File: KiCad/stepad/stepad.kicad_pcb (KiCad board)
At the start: 2 copper layers, 111.2 x 35 mm, 69 parts, among them J1 TYPE-C-31-M12_13_EDITED, J2 Conn_01x03, SW1 MX_Lekker, SW2 MX_Lekker, SW3 MX_Lekker, SW4 MX_Lekker, SW5 SW_Push, SW6 SW_Push, U1 AH49-E, U2 AH49-E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

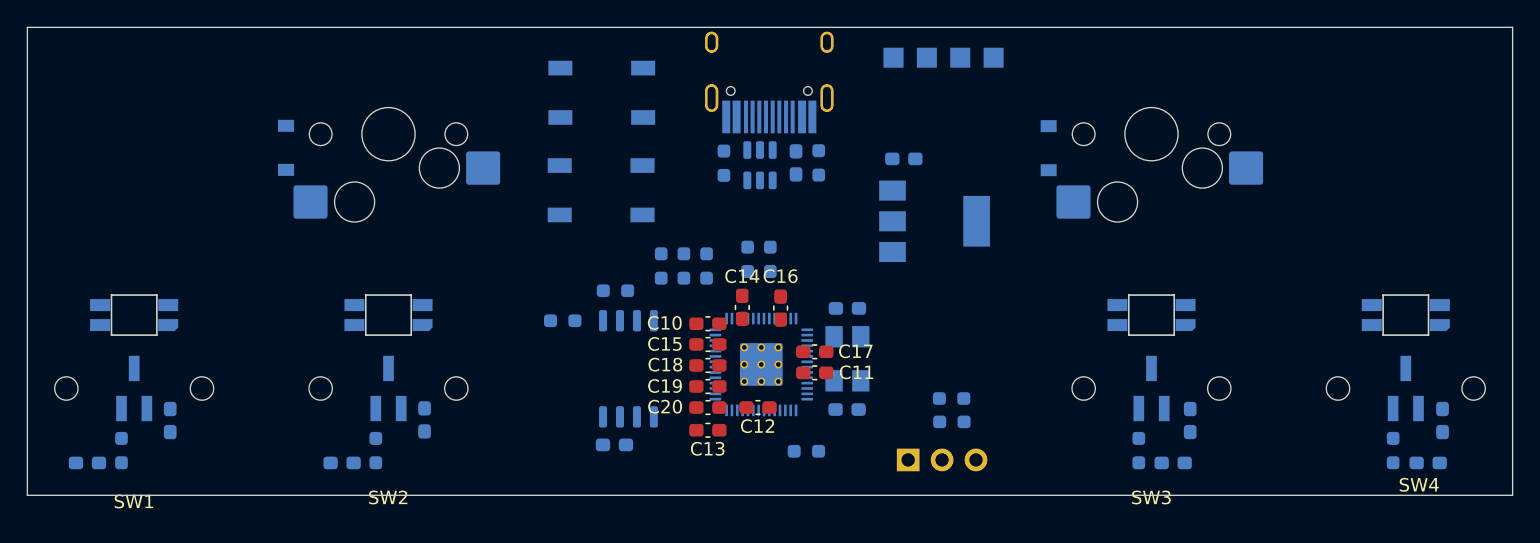
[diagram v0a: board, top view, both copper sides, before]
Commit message: Finished initial layout
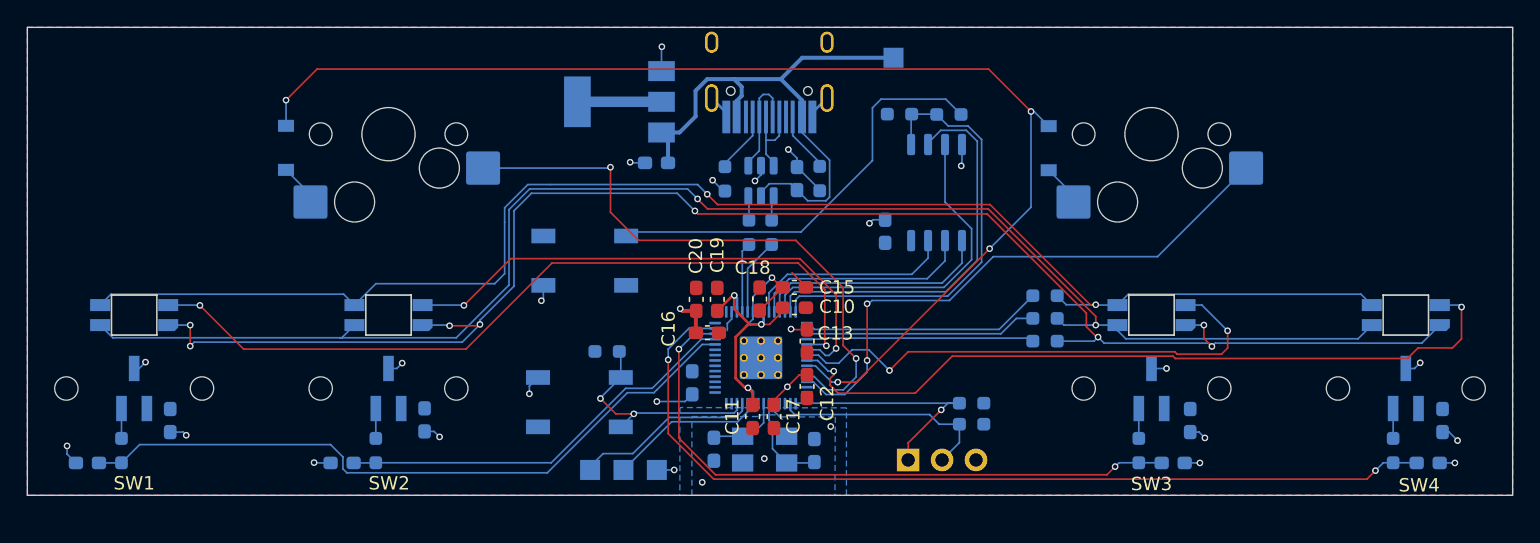
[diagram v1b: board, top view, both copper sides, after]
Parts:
- C14: moved to B.Cu
- moved TP2 39.9 mm to (184.6, 78.1)
- moved TP3 39.9 mm to (187.1, 78.1)
- moved TP4 39.9 mm to (189.6, 78.1)
- moved R11 32.8 mm to (211.4, 51.5), turned to 180 degrees
- moved R5 28.8 mm to (218.6, 65.0), turned to 0 degrees
- moved R6 27.3 mm to (218.6, 66.8), turned to 0 degrees
- moved U6 26.6 mm to (210.5, 57.3)
- moved R7 26.0 mm to (218.6, 68.5), turned to 180 degrees
- moved C21 25.8 mm to (206.7, 60.2), turned to -90 degrees
- moved U5 25.2 mm to (186.8, 50.5), turned to 180 degrees
- moved R10 25.1 mm to (207.7, 51.5), turned to 180 degrees
- moved SW6 23.2 mm to (183.8, 73.0)
- moved C5 18.5 mm to (189.5, 55.1), turned to 0 degrees
- moved R16 16.7 mm to (185.8, 69.2)
- moved C22 10.9 mm to (201.3, 76.7), turned to -90 degrees
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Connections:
- SW6 pad 2: GND -> (no net)
- SW6 pad 3: (no net) -> /RESET
- SW6 pad 4: (no net) -> GND
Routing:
- net Net-(D1-Pad1): track 0.00 -> 121.8 mm, vias 0 -> 8
- net Net-(D1-Pad2): track 0.00 -> 113.8 mm, vias 0 -> 2
- net Net-(D1-Pad3): track 0.00 -> 110.1 mm, vias 0 -> 2
- net K_ROW: track 0.00 -> 91.7 mm, vias 0 -> 4
- net SW4: track 0.00 -> 68.5 mm, vias 0 -> 2
- net COL1: track 0.00 -> 59.8 mm, vias 0 -> 2
- net COL4: track 0.00 -> 57.0 mm, vias 0 -> 2
- net SW1: track 0.00 -> 52.1 mm
- net SW3: track 0.00 -> 47.5 mm, vias 0 -> 2
- net K_COL0: track 0.00 -> 44.3 mm, vias 0 -> 2
- net K_COL1: track 0.00 -> 43.3 mm, vias 0 -> 2
- net +5V: track 0.00 -> 43.2 mm
- net GND: track 0.00 -> 41.0 mm, vias 0 -> 26
- net COL2: track 0.00 -> 40.2 mm, vias 0 -> 2
- net COL3: track 0.00 -> 38.9 mm, vias 0 -> 2
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- added copper zone on B.Cu, net +3.3VA
- added copper zone on B.Cu, net GND
- added copper zone on F.Cu, net GND

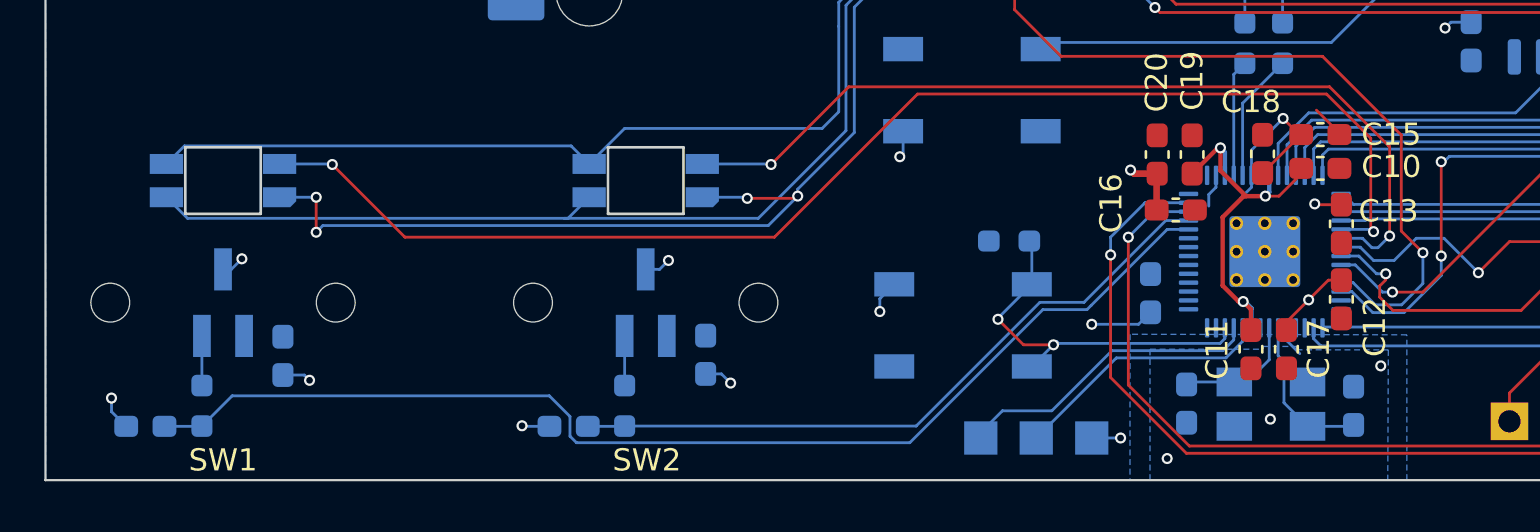
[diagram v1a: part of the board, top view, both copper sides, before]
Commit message: Adding part numbers and updating some footprints
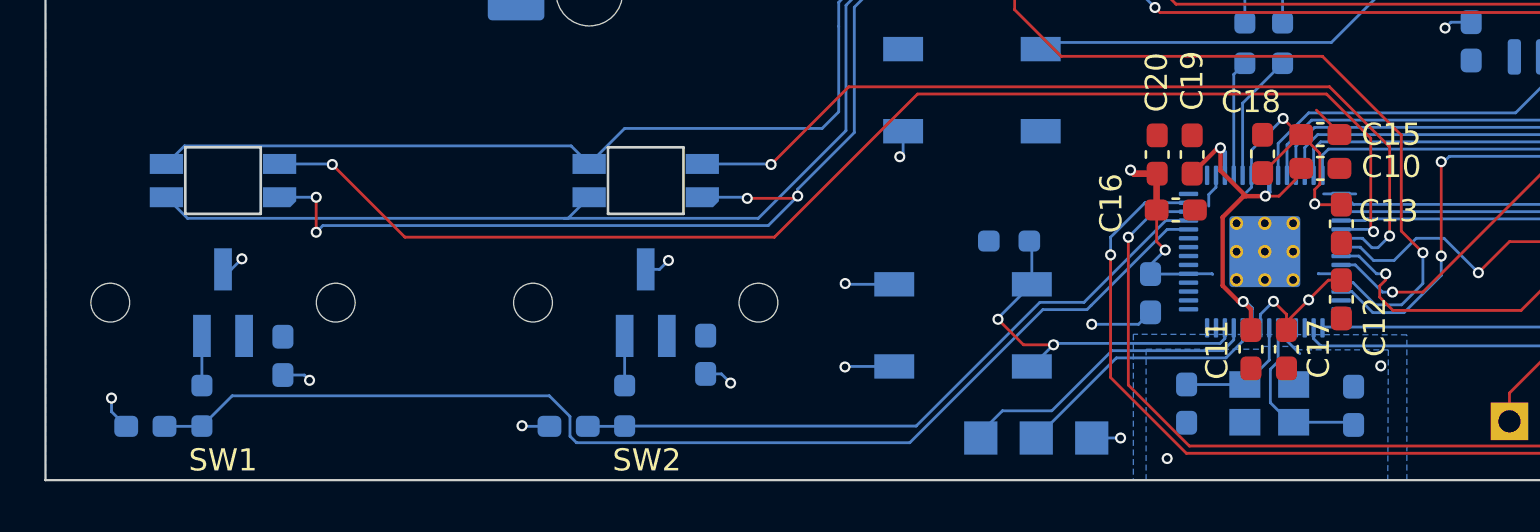
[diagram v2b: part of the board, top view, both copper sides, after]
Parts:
- Y1: footprint Crystal:Crystal_SMD_5032-4Pin_5.0x3.2mm -> Crystal:Crystal_SMD_3225-4Pin_3.2x2.5mm
- moved Y1 0.08 mm to (197.6, 76.5)
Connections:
- SW6 pad 2: (no net) -> GND
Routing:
- net +3.3VA: track 23.6 -> 38.7 mm, vias 4 -> 6
- net GND: track 41.0 -> 44.0 mm
- net /XOUT: track 5.62 -> 6.39 mm
- net /XIN: track 7.09 -> 7.68 mm

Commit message: Updating gerbers and adding firmware folder
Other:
- board text added: "RX"
- board text added: "TX"
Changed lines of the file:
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@@
   )
   (gr_rect (start 253.65 80) (end 142.4 44.95) (layer "Edge.Cuts") (width 0.1) (fill none))
+  (gr_text "RX" (at 210.89 75.23) (layer "F.SilkS")
+    (effects (font (size 1 1) (thickness 0.15)))
+  )
+  (gr_text "TX" (at 208.27 75.27) (layer "F.SilkS")
+    (effects (font (size 1 1) (thickness 0.15)))
+  )
   (segment (start 198.175 63.7) (end 198.9 64.425) (width 0.127) (layer "F.Cu") (net 1))
   (segment (start 192.475 67.825) (end 192.475 66.2125) (width 0.3) (layer "F.Cu") (net 1))
@@
   (segment (start 243.375 78.15) (end 243.9625 77.5625) (width 0.127) (layer "B.Cu") (net 6))
   (segment (start 195.2375 65.025) (end 194.075 66.1875) (width 0.2) (layer "F.Cu") (net 7))
-  (segment (start 198.9875 66.2) (end 197.9875 67.2) (width 0.127) (layer "F.Cu") (net 7))
   (segment (start 196.166793 71.95) (end 195.450479 71.233686) (width 0.2) (layer "F.Cu") (net 7))
   (segment (start 196.4 67.2) (end 196.5 67.2) (width 0.2) (layer "F.Cu") (net 7))
+  (segment (start 197.35 67.4) (end 196.7 67.4) (width 0.2) (layer "F.Cu") (net 7))
   (segment (start 196.5 67.2) (end 195.35 66.05) (width 0.2) (layer "F.Cu") (net 7))
   (segment (start 195.35 66.05) (end 195.35 65.025) (width 0.2) (layer "F.Cu") (net 7))
-  (segment (start 197.375 67.2) (end 196.5 67.2) (width 0.2) (layer "F.Cu") (net 7))
+  (segment (start 198.9875 66.2) (end 198.9875 65.95) (width 0.127) (layer "F.Cu") (net 7))
   (segment (start 195.450479 68.149521) (end 196.4 67.2) (width 0.2) (layer "F.Cu") (net 7))
   (segment (start 195.450479 71.233686) (end 195.450479 68.149521) (width 0.2) (layer "F.Cu") (net 7))
   (segment (start 196.375 71.95) (end 196.725 72.3) (width 0.2) (layer "F.Cu") (net 7))
-  (segment (start 198.9875 65.95) (end 198.9875 66.2) (width 0.127) (layer "F.Cu") (net 7))
+  (segment (start 196.7 67.4) (end 196.5 67.2) (width 0.2) (layer "F.Cu") (net 7))
   (segment (start 195.35 65.025) (end 195.2375 65.025) (width 0.2) (layer "F.Cu") (net 7))
   (segment (start 196.725 72.3) (end 196.725 73.2375) (width 0.2) (layer "F.Cu") (net 7))
   (segment (start 196.375 71.95) (end 196.166793 71.95) (width 0.2) (layer "F.Cu") (net 7))
-  (segment (start 197.375 67.2) (end 197.9875 67.2) (width 0.127) (layer "F.Cu") (net 7))
+  (segment (start 197.7875 67.4) (end 198.9875 66.2) (width 0.127) (layer "F.Cu") (net 7))
+  (segment (start 197.35 67.4) (end 197.7875 67.4) (width 0.127) (layer "F.Cu") (net 7))
   (via (at 195.35 65.025) (size 0.5) (drill 0.3) (layers "F.Cu" "B.Cu") (net 7))
-  (via (at 197.375 67.2) (size 0.5) (drill 0.3) (layers "F.Cu" "B.Cu") (net 7))
+  (via (at 197.35 67.4) (size 0.5) (drill 0.3) (layers "F.Cu" "B.Cu") (net 7))
   (via (at 196.375 71.95) (size 0.5) (drill 0.3) (layers "F.Cu" "B.Cu") (net 7))
-  (segment (start 197.55 67.025) (end 197.55 66.2625) (width 0.2) (layer "B.Cu") (net 7))
   (segment (start 195.55 66.2625) (end 195.55 65.225) (width 0.2) (layer "B.Cu") (net 7))
   (segment (start 196.375 71.95) (end 196.45 71.95) (width 0.2) (layer "B.Cu") (net 7))
   (segment (start 196.75 72.25) (end 196.75 73.1375) (width 0.2) (layer "B.Cu") (net 7))
+  (segment (start 197.55 67.2) (end 197.55 66.2625) (width 0.2) (layer "B.Cu") (net 7))
   (segment (start 196.45 71.95) (end 196.75 72.25) (width 0.2) (layer "B.Cu") (net 7))
   (segment (start 195.55 65.225) (end 195.35 65.025) (width 0.2) (layer "B.Cu") (net 7))
-  (segment (start 197.375 67.2) (end 197.55 67.025) (width 0.2) (layer "B.Cu") (net 7))
+  (segment (start 197.35 67.4) (end 197.55 67.2) (width 0.2) (layer "B.Cu") (net 7))
   (segment (start 190.46046 74.16454) (end 187.75 76.875) (width 0.127) (layer "B.Cu") (net 8))
   (segment (start 195.464906 74.16454) (end 190.46046 74.16454) (width 0.127) (layer "B.Cu") (net 8))
